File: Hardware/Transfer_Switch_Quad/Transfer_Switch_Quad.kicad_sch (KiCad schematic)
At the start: 30 parts, among them J1 Relays, J10 RF1, J6 RF2, J7 RF3, J8 AMP, J9 RF4, K10 G2RL-1-E, K11 G2RL-1-E, K12 G2RL-1-E, K13 G2RL-1-E, K14 G2RL-1-E, K15 G2RL-1-E, K16 G2RL-1-E, K9 G2RL-1-E

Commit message: Updated presentation using LibreOffice Tweaked appearance of schematic Added datasheets
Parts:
- TP2: renamed from TP24; value Jump2 -> Coax2
- TP3: renamed from TP16; value Jump3 -> Coax3
- TP5: value Jump1 -> Coax1
- TP8: renamed from TP20; value Jump4 -> Coax4
- renumbered C4 to C1, C3 to C2, C2 to C3, C1 to C4, D3 to D1, D4 to D2, D2 to D3, D1 to D4, J7 to J1, J6 to J2, J8 to J3, J9 to J4, J10 to J5, J1 to J6, K16 to K1, K14 to K2, K12 to K3, K9 to K4, K11 to K5, K10 to K6, K13 to K7, K15 to K8, TP7 to TP1, TP17 to TP4, TP25 to TP7
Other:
- moved on the sheet: D1, D2, D3, D4, J1, K1, K2, K3, K4, K5, K6, K7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

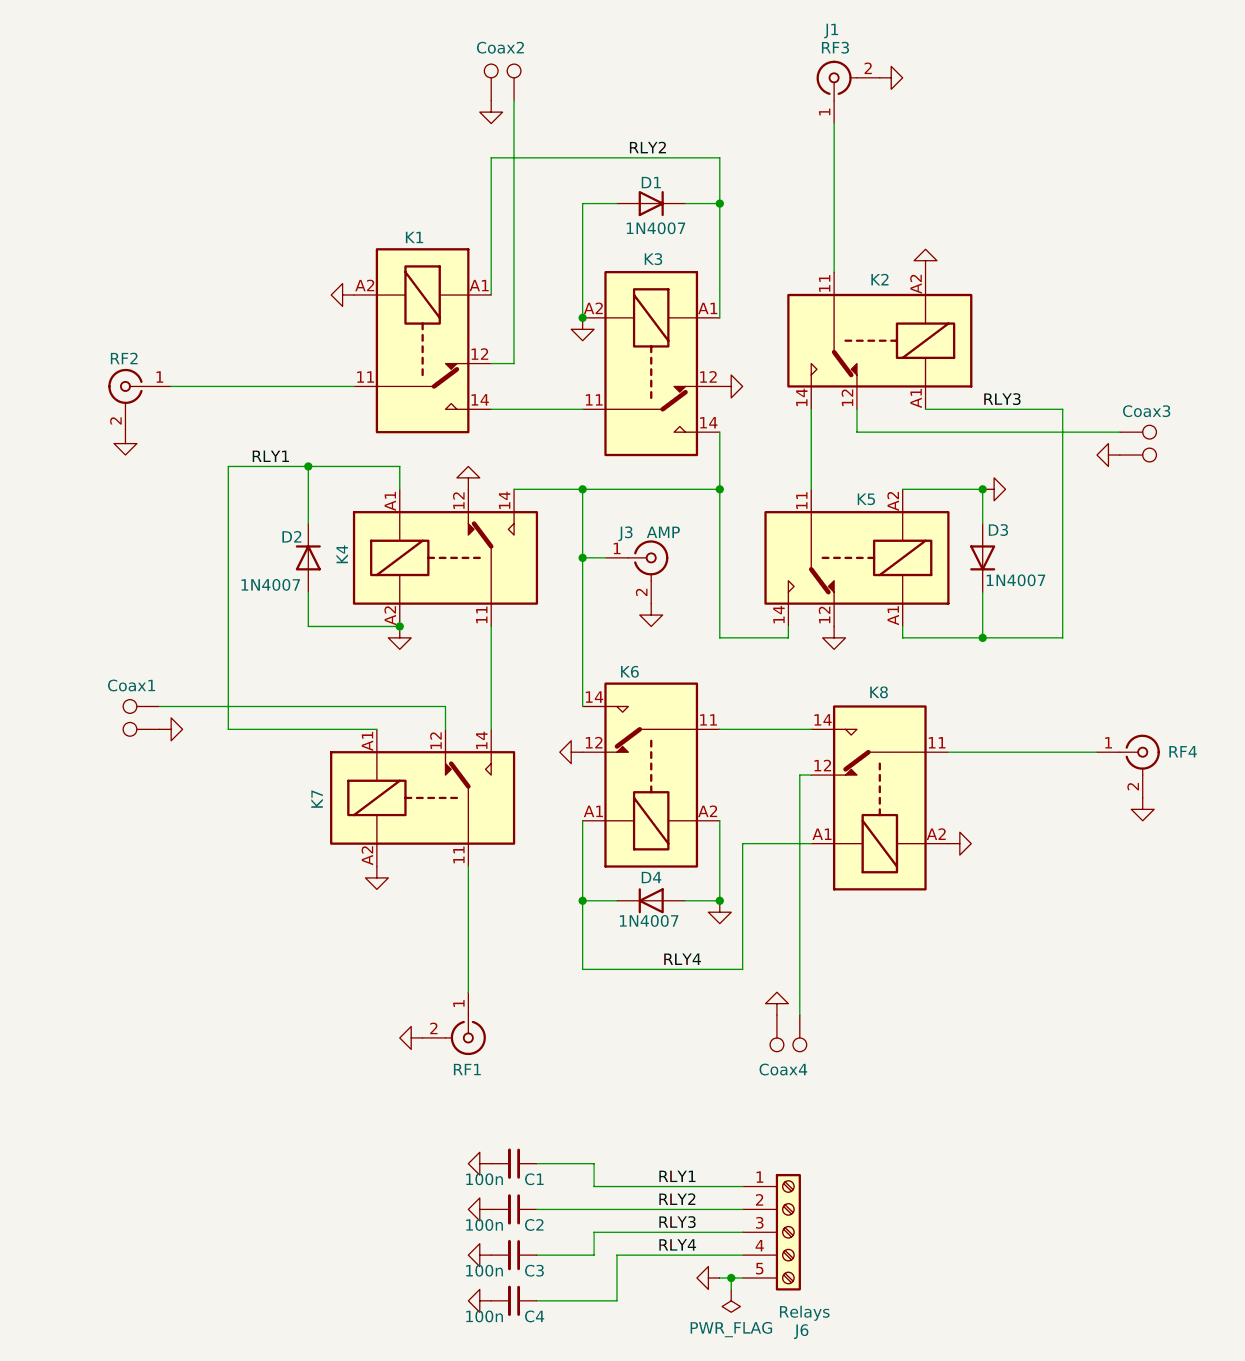
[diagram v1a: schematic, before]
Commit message: SO-239 mount directly to the bottom of the pcb, so large hole and jumper to pad
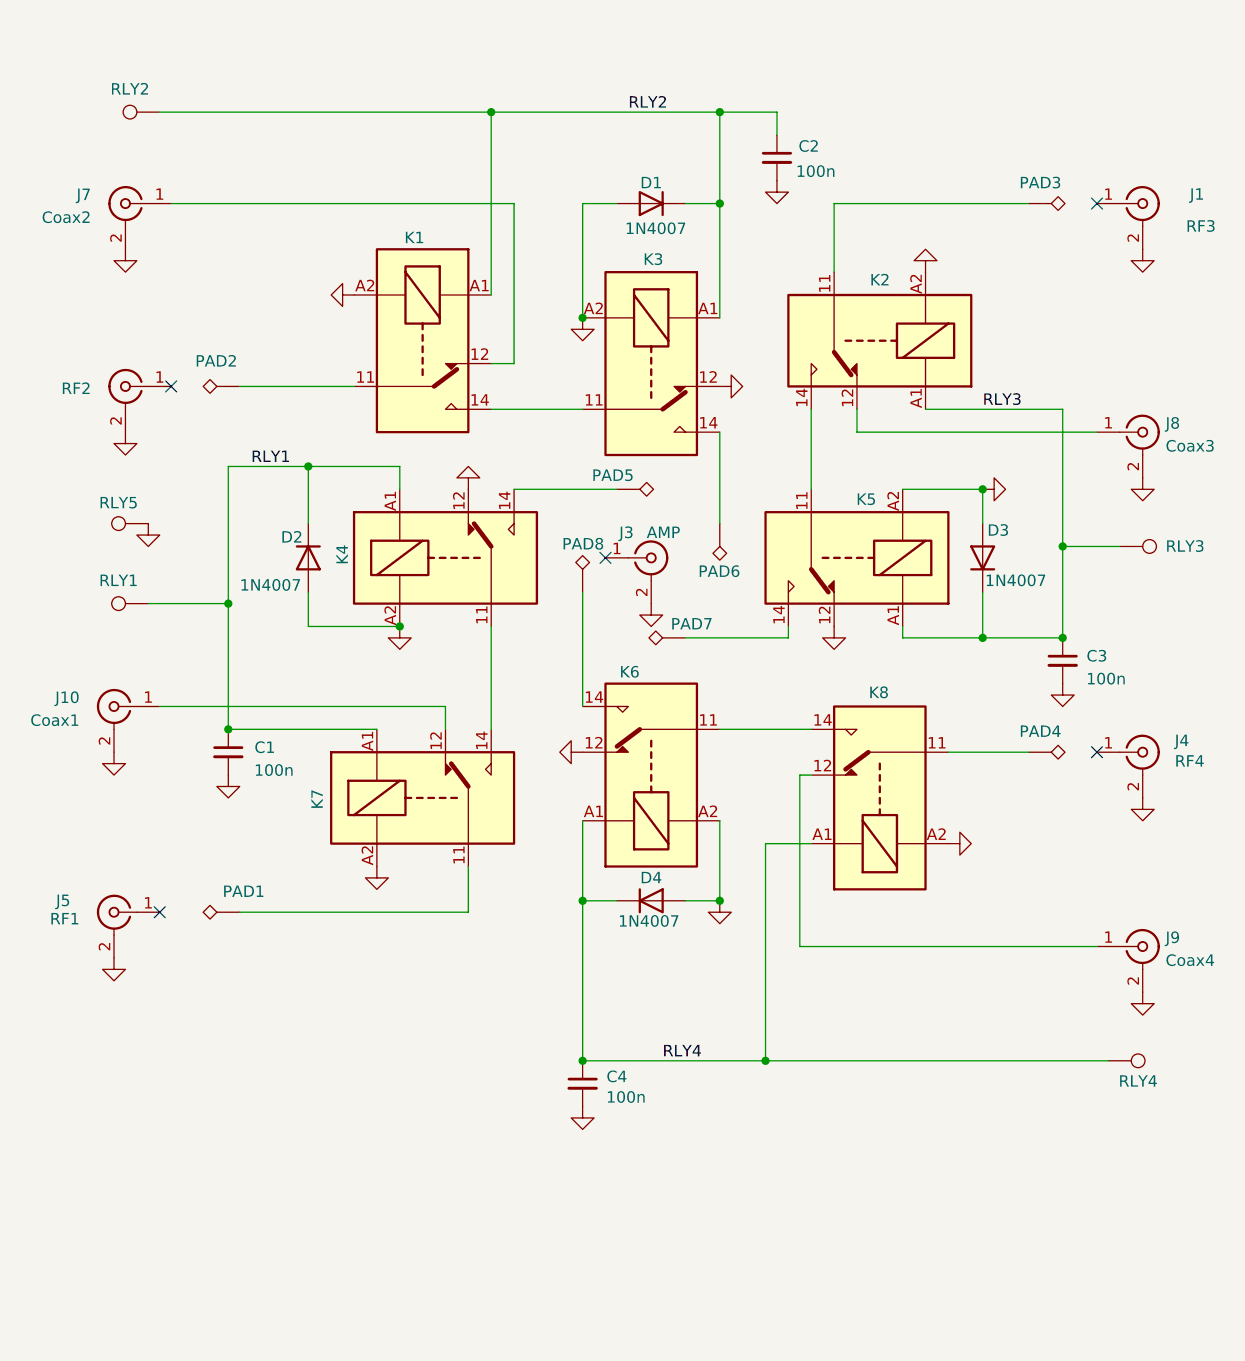
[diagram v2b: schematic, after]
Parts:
- removed J6: Relays, TerminalBlock:TerminalBlock_Xinya_XY308-2.54-5P_1x05_P2.54mm_Horizontal, symbol Connector:Screw_Terminal_01x05
- removed TP1, TP4, TP6, TP7: TestPoint, TestPoint:TestPoint_Pad_2.5x2.5mm, symbol Connector:TestPoint
- removed TP2: Coax2, TestPoint:TestPoint_Pad_2.5x2.5mm, symbol Connector:TestPoint
- removed TP3: Coax3, TestPoint:TestPoint_Pad_2.5x2.5mm, symbol Connector:TestPoint
- removed TP5: Coax1, TestPoint:TestPoint_Pad_2.5x2.5mm, symbol Connector:TestPoint
- removed TP8: Coax4, TestPoint:TestPoint_Pad_2.5x2.5mm, symbol Connector:TestPoint
- added J10: Coax1, Connector_Coaxial:SMA_Amphenol_901-144_Vertical, symbol Connector:Conn_Coaxial
- added J7: Coax2, Connector_Coaxial:SMA_Amphenol_901-144_Vertical, symbol Connector:Conn_Coaxial
- added J8: Coax3, Connector_Coaxial:SMA_Amphenol_901-144_Vertical, symbol Connector:Conn_Coaxial
- added J9: Coax4, Connector_Coaxial:SMA_Amphenol_901-144_Vertical, symbol Connector:Conn_Coaxial
- added PAD1, PAD2, PAD3, PAD4, PAD5, PAD6, PAD7, PAD8: PAD2X4, Connector_Wire:SolderWirePad_1x01_SMD_2x4mm, symbol Connector:TestPoint_Alt
- added RLY1, RLY2, RLY3, RLY4, RLY5: ~, Connector_Wire:SolderWire-0.25sqmm_1x01_D0.65mm_OD2mm, symbol Connector:TestPoint
- J1, J2, J3, J4, J5: footprint Relay_4to1:UHF_SO-239_Pin -> Relay_4to1:UHF_SO-239_hole
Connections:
- net GND: now also J10.2 (Ext), J7.2 (Ext), J8.2 (Ext), J9.2 (Ext), RLY5.1
- net RLY1: now also RLY1.1
- net RLY2: now also RLY2.1
- net RLY3: now also RLY3.1
- net RLY4: now also RLY4.1
- net at J5.1 (In): no longer K7.11
- net at J4.1 (In): no longer K8.11
- net at J1.1 (In): no longer K2.11
- net at K2.12: now also J8.1 (In)
- net at K7.12: now also J10.1 (In)
- net at K1.12: now also J7.1 (In)
- net at K1.11: now also PAD2.1; no longer J2.1 (In)
- net at K8.12: now also J9.1 (In)
- new net: K4.14, PAD5.1
- new net: K5.14, PAD7.1
- new net: K7.11, PAD1.1
- new net: K8.11, PAD4.1
- new net: K3.14, PAD6.1
- new net: K6.14, PAD8.1
- new net: K2.11, PAD3.1
- now unconnected: J3.1 (In)
- no-connect marks 0 -> 5
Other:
- moved on the sheet: C1, C2, C3, C4, J1
